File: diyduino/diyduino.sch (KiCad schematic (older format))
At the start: 18 parts, among them U1 ATMEGA328-PU, U2 L7805, Y1 16MHz

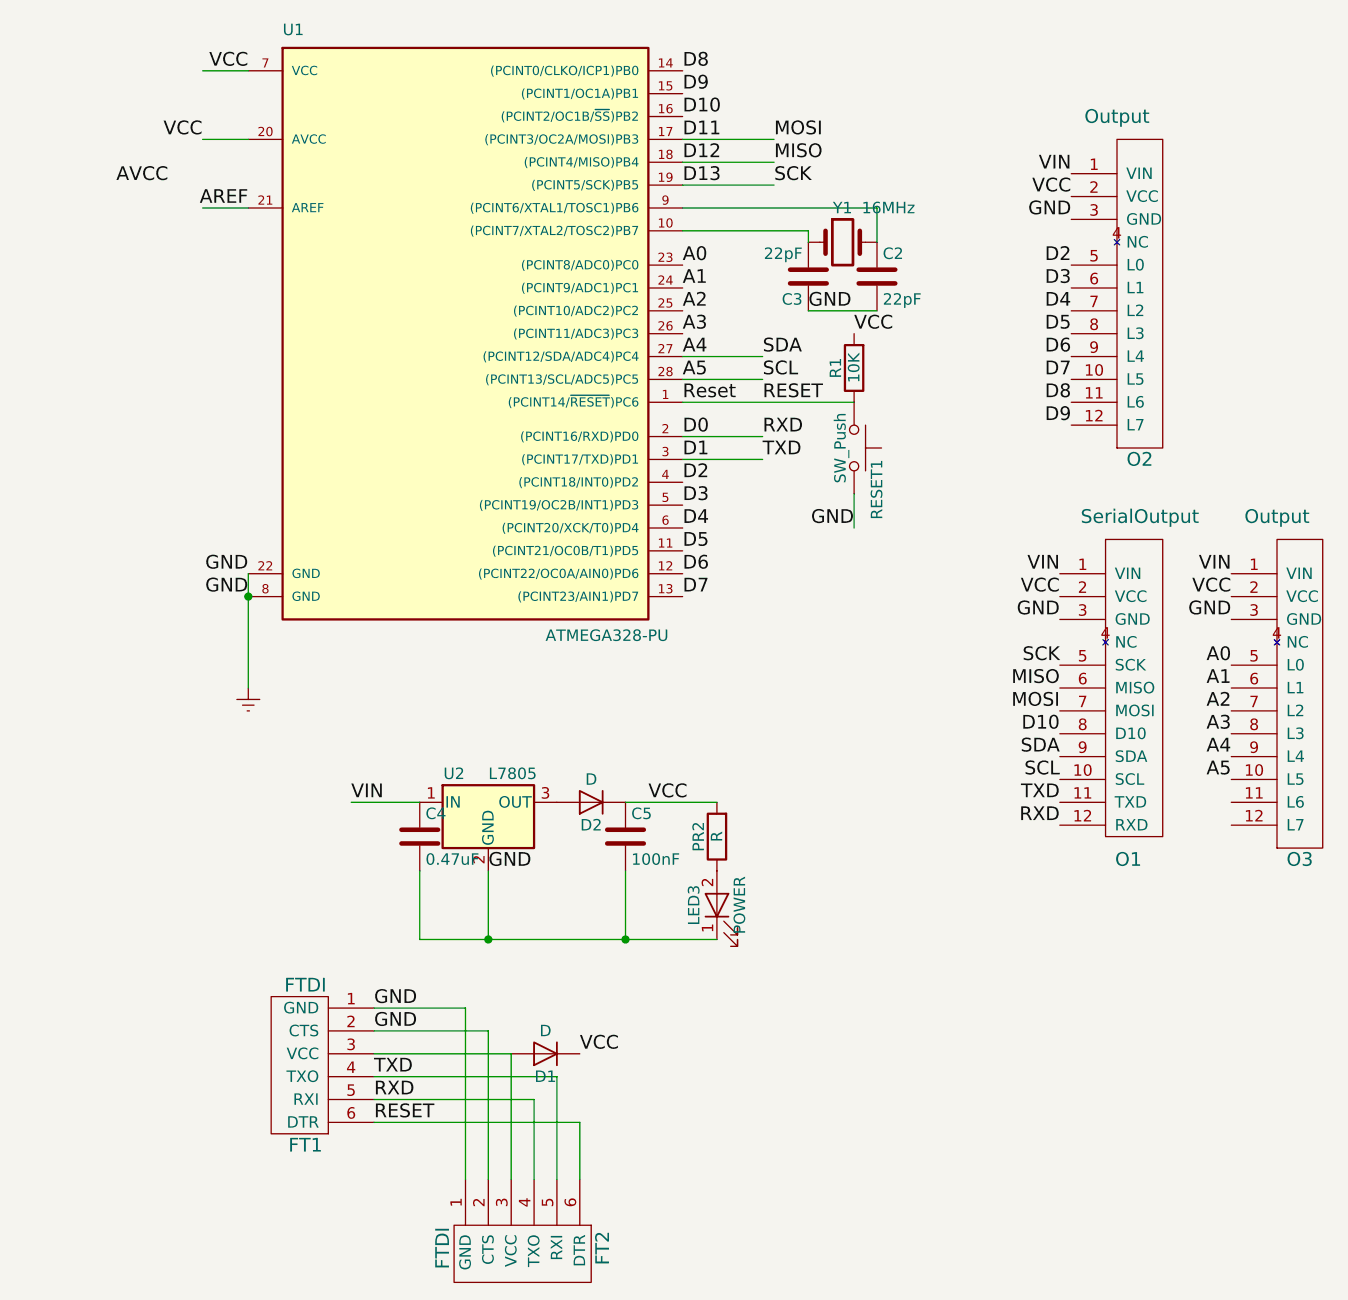
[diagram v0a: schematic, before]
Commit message: More work to ensure there are no errors from KiCAD's schematic checker. Fixed the multiplexer module, so that all 7 slaves will work (only 6 were working, due to a missing VCC to the "Next Output").
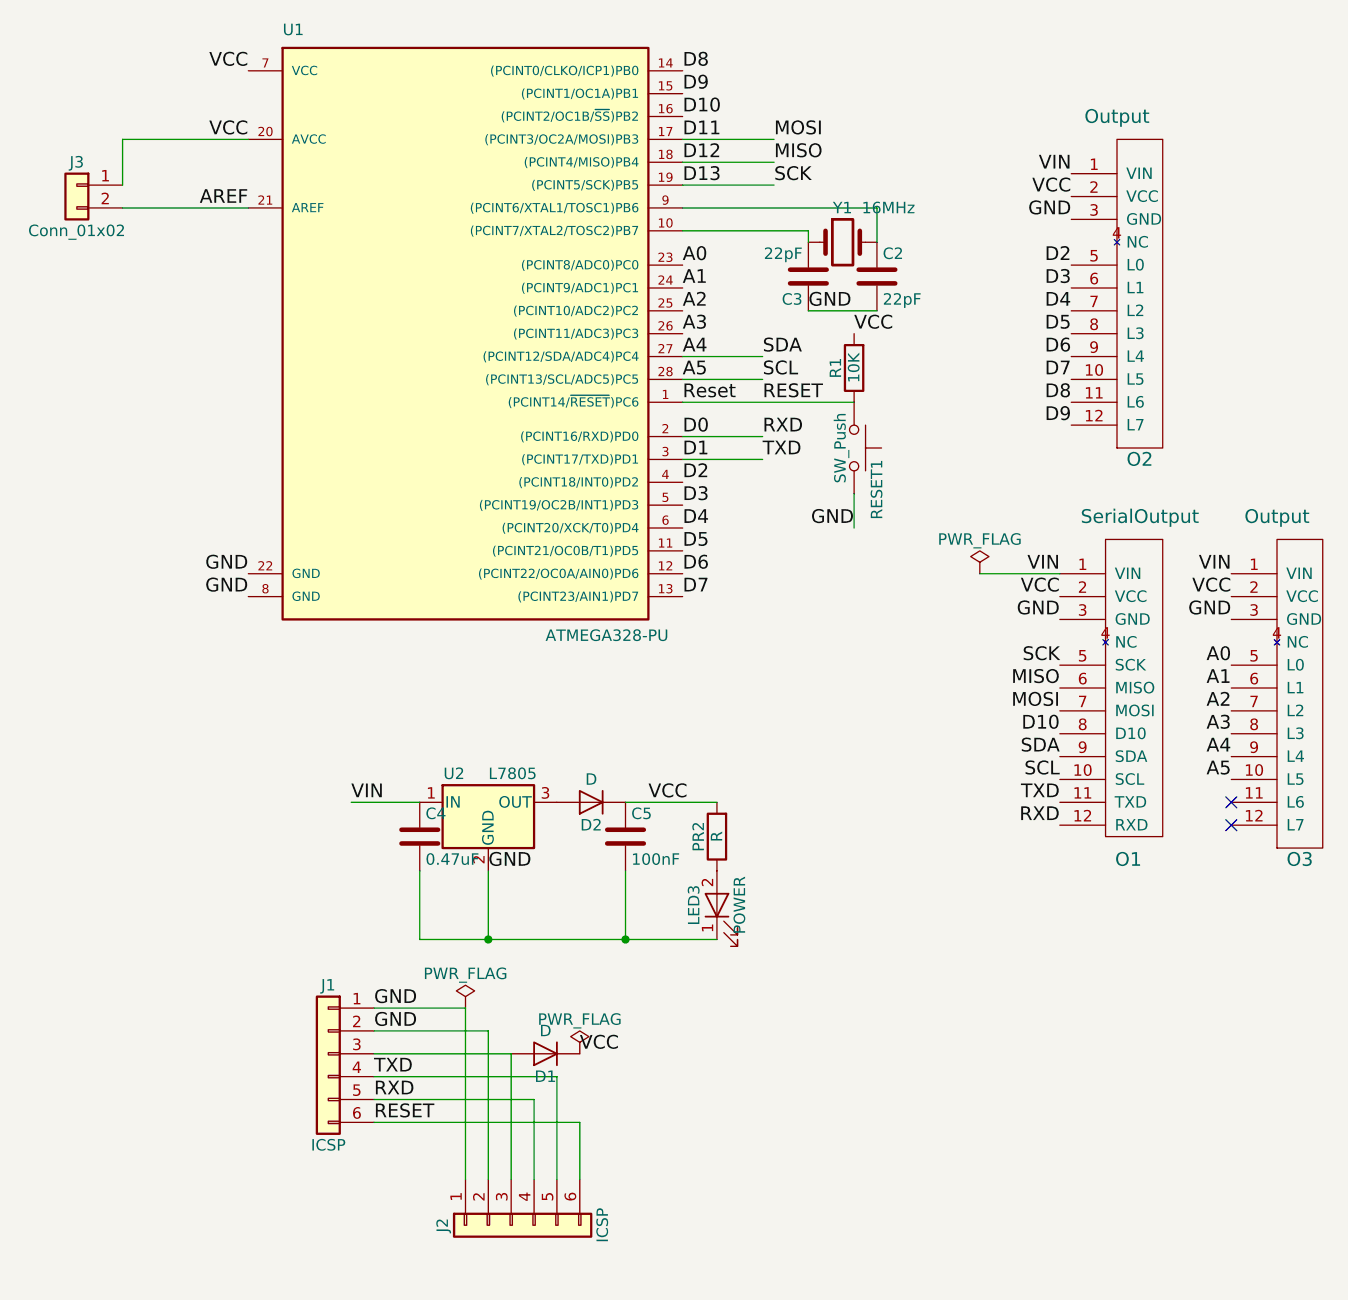
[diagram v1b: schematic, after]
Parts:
- removed FT1, FT2: FTDI, Pin_Headers:Pin_Header_Straight_1x06_Pitch2.54mm, symbol FTDI
- added J1, J2: ICSP, Pin_Headers:Pin_Header_Straight_1x06_Pitch2.54mm, symbol Conn_01x06
- added J3: Conn_01x02, Pin_Headers:Pin_Header_Straight_1x02_Pitch2.54mm, symbol Conn_01x02
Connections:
- net labels removed: AVCC, Earth
- no-connect marks 0 -> 2
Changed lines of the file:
@@
 LIBS:eplay
 LIBS:arduino
-LIBS:diyduino-cache
 EELAYER 25 0
 EELAYER END
@@
 Text Label 1750 1600 2    60   ~ 0
 AREF
-Text Label 1400 1500 2    60   ~ 0
-AVCC
 Text Label 3650 2800 0    60   ~ 0
 D2
@@
 TXD
 $Comp
-L Earth #PWR01
-U 1 1 5ABE6C80
-P 1750 3700
-F 0 "#PWR01" H 1750 3450 50  0001 C CNN
-F 1 "Earth" H 1750 3550 50  0001 C CNN
-F 2 "" H 1750 3700 50  0001 C CNN
-F 3 "" H 1750 3700 50  0001 C CNN
-	1    1750 3700
-	1    0    0    -1
-$EndComp
-$Comp
 L ATMEGA328-PU U1
 U 1 1 5ABEDA30
@@
 Text Label 4400 3000 2    60   ~ 0
 GND
-Text Label 1550 1300 2    60   ~ 0
+Text Label 1750 1300 2    60   ~ 0
 VCC
 $Comp
@@
 F 3 "" H 2800 4150 50  0001 C CNN
 	1    2800 4200
-	1    0    0    -1
-$EndComp
-$Comp
-L FTDI FT1
-U 1 1 5AC1B1CC
-P 2000 5350
-F 0 "FT1" H 2000 5000 60  0000 C CNN
-F 1 "FTDI" H 2000 5700 60  0000 C CNN
-F 2 "Pin_Headers:Pin_Header_Straight_1x06_Pitch2.54mm" H 2000 5350 60  0001 C CNN
-F 3 "" H 2000 5350 60  0001 C CNN
-	1    2000 5350
 	1    0    0    -1
 $EndComp
@@
 Wire Wire Line
 	3650 2700 4000 2700
-Connection ~ 1750 3300
-Wire Wire Line
-	1750 3200 1750 3700
 Wire Wire Line
 	3650 2450 4400 2450
@@
 Wire Wire Line
 	3650 1700 4200 1700
-Wire Wire Line
-	1750 1600 1550 1600
-Wire Wire Line
-	1550 1000 1750 1000
-Wire Wire Line
-	1750 1300 1550 1300
 Wire Wire Line
 	2200 4200 2500 4200
@@
 	3400 4500 3400 4800
 Connection ~ 3400 4800
-$Comp
-L FTDI FT2
-U 1 1 5AC50B3D
-P 2950 6150
-F 0 "FT2" H 2950 5800 60  0000 C CNN
-F 1 "FTDI" H 2950 6500 60  0000 C CNN
-F 2 "Pin_Headers:Pin_Header_Straight_1x06_Pitch2.54mm" H 2950 6150 60  0001 C CNN
-F 3 "" H 2950 6150 60  0001 C CNN
-	1    2950 6150
-	0    -1   -1   0
-$EndComp
 Wire Wire Line
 	2300 5600 3200 5600
@@
 Wire Wire Line
 	3000 5500 3000 5850
+$Comp
+L PWR_FLAG #FLG01
+U 1 1 5AFEA938
+P 2700 5100
+F 0 "#FLG01" H 2700 5175 50  0001 C CNN
+F 1 "PWR_FLAG" H 2700 5250 50  0000 C CNN
+F 2 "" H 2700 5100 50  0001 C CNN
+F 3 "" H 2700 5100 50  0001 C CNN
+	1    2700 5100
+	1    0    0    -1
+$EndComp
+$Comp
+L PWR_FLAG #FLG02
+U 1 1 5AFEA970
+P 3200 5300
+F 0 "#FLG02" H 3200 5375 50  0001 C CNN
+F 1 "PWR_FLAG" H 3200 5450 50  0000 C CNN
+F 2 "" H 3200 5300 50  0001 C CNN
+F 3 "" H 3200 5300 50  0001 C CNN
+	1    3200 5300
+	1    0    0    -1
+$EndComp
+$Comp
+L Conn_01x06 J1
+U 1 1 5AFEAAC5
+P 2100 5300
+F 0 "J1" H 2100 5600 50  0000 C CNN
+F 1 "ICSP" H 2100 4900 50  0000 C CNN
+F 2 "Pin_Headers:Pin_Header_Straight_1x06_Pitch2.54mm" H 2100 5300 50  0001 C CNN
+F 3 "" H 2100 5300 50  0001 C CNN
+	1    2100 5300
+	-1   0    0    -1
+$EndComp
+$Comp
+L Conn_01x06 J2
+U 1 1 5AFEAC6B
+P 2900 6050
+F 0 "J2" H 2900 6350 50  0000 C CNN
+F 1 "ICSP" H 2900 5650 50  0000 C CNN
+F 2 "Pin_Headers:Pin_Header_Straight_1x06_Pitch2.54mm" H 2900 6050 50  0001 C CNN
+F 3 "" H 2900 6050 50  0001 C CNN
+	1    2900 6050
+	0    -1   1    0
+$EndComp
+NoConn ~ 6050 4200
+NoConn ~ 6050 4300
+$Comp
+L PWR_FLAG #FLG03
+U 1 1 5AFEB6CD
+P 4950 3200
+F 0 "#FLG03" H 4950 3275 50  0001 C CNN
+F 1 "PWR_FLAG" H 4950 3350 50  0000 C CNN
+F 2 "" H 4950 3200 50  0001 C CNN
+F 3 "" H 4950 3200 50  0001 C CNN
+	1    4950 3200
+	1    0    0    -1
+$EndComp
+Wire Wire Line
+	5300 3200 4950 3200
+$Comp
+L Conn_01x02 J3
+U 1 1 5AFEC722
+P 1000 1500
+F 0 "J3" H 1000 1600 50  0000 C CNN
+F 1 "Conn_01x02" H 1000 1300 50  0000 C CNN
+F 2 "Pin_Headers:Pin_Header_Straight_1x02_Pitch2.54mm" H 1000 1500 50  0001 C CNN
+F 3 "" H 1000 1500 50  0001 C CNN
+	1    1000 1500
+	-1   0    0    -1
+$EndComp
+Wire Wire Line
+	1200 1600 1750 1600
+Wire Wire Line
+	1750 1300 1200 1300
+Wire Wire Line
+	1200 1300 1200 1500
 $EndSCHEMATC
